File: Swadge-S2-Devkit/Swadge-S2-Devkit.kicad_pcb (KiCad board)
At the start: 2 copper layers, 134 x 100 mm, 103 parts, among them J1 CurrentMonitor, J10 LCD18, J11 LCD28, J2 DEBUG_BANK_C, J3 DEBUG_BANK_B, J4 DEBUG_BANK_A, J5 MICSEL, J6 TRYMIC, J7 LEDK_J, J8 IM0, M1 Motor_DC, P1 USB_C_Plug_USB2.0, Q1 Q_N_FET, Q2 AP2003_PN_FET, Q3 AP2003_PN_FET, Q4 AP2003_PN_FET, SW1 4-1437565-2, SW13 touch-ring-6, SW14 SW_SPDT, SW2 4-1437565-2, SW3 4-1437565-2, SW4 4-1437565-2, SW5 4-1437565-2, SW6 4-1437565-2, SW7 4-1437565-2, SW8 4-1437565-2, SW9 4-1437565-2, U1 ESP32-S2-SOLO, U10 GENERIC_LDO_GOI, U11 LCD_240x240_1.3_12, U12 LCD_135x240_1.14_13, U15 LCD_240x240_1.54_12, U2 BUS_PCIexpress, U3 MT3410, U4 GS321-TR, U5 QMA7981, U6 INGHAi_GSPK2308P-8R0.5W, U7 TFT-1.14, U8 TFT_DISPLAY, U9 GENERIC_LDO_1.8

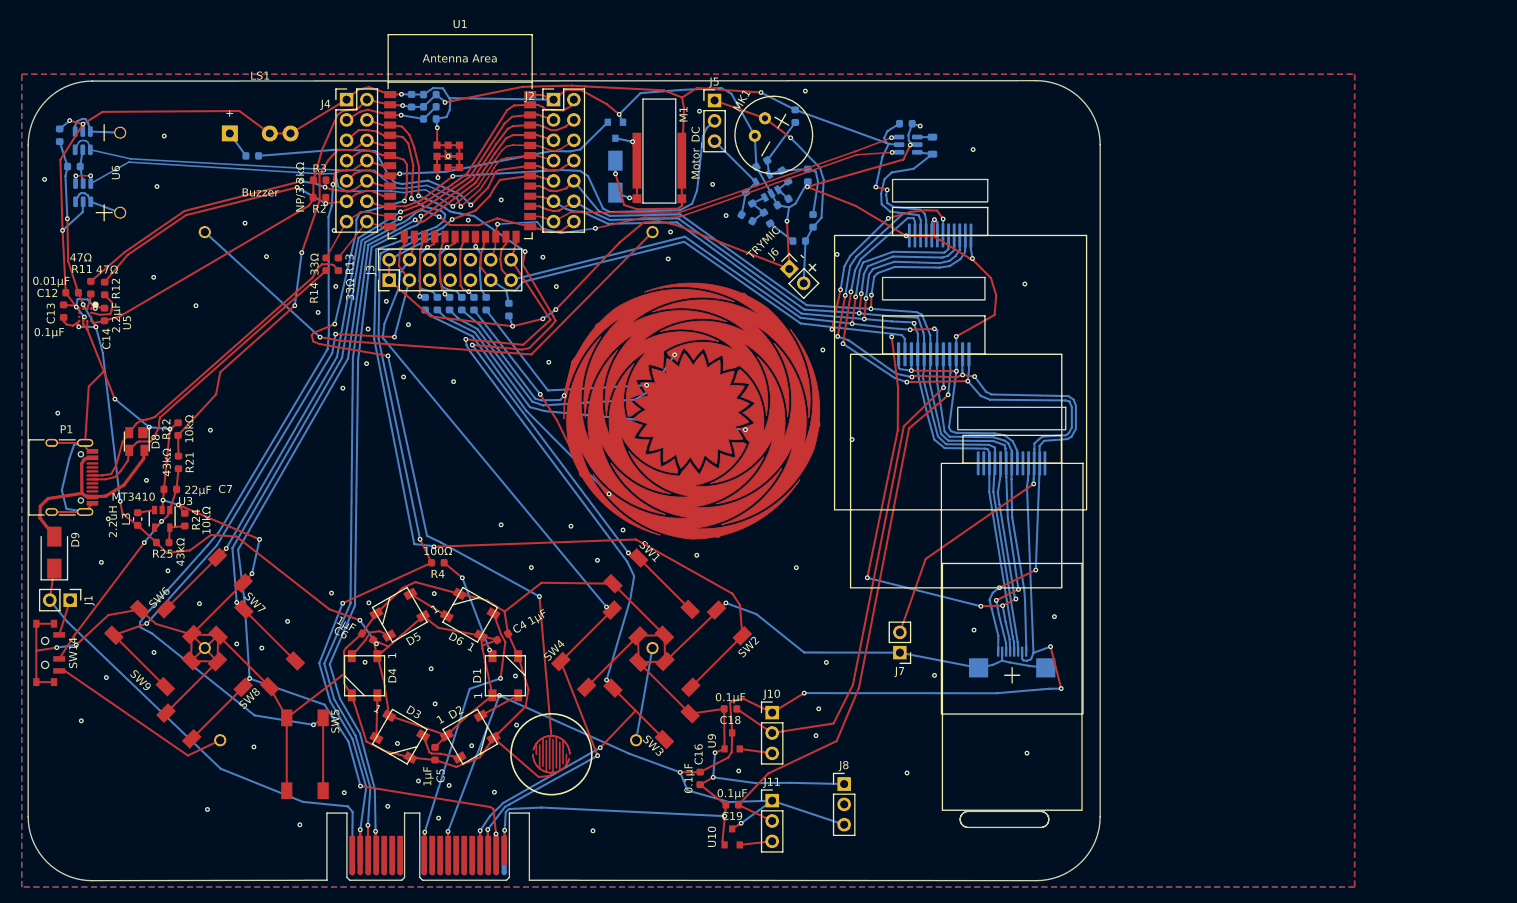
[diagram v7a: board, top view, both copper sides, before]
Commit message: Removed unused parts of schematic. Replaced out of stock parts. Rerouted batteries, LDOs
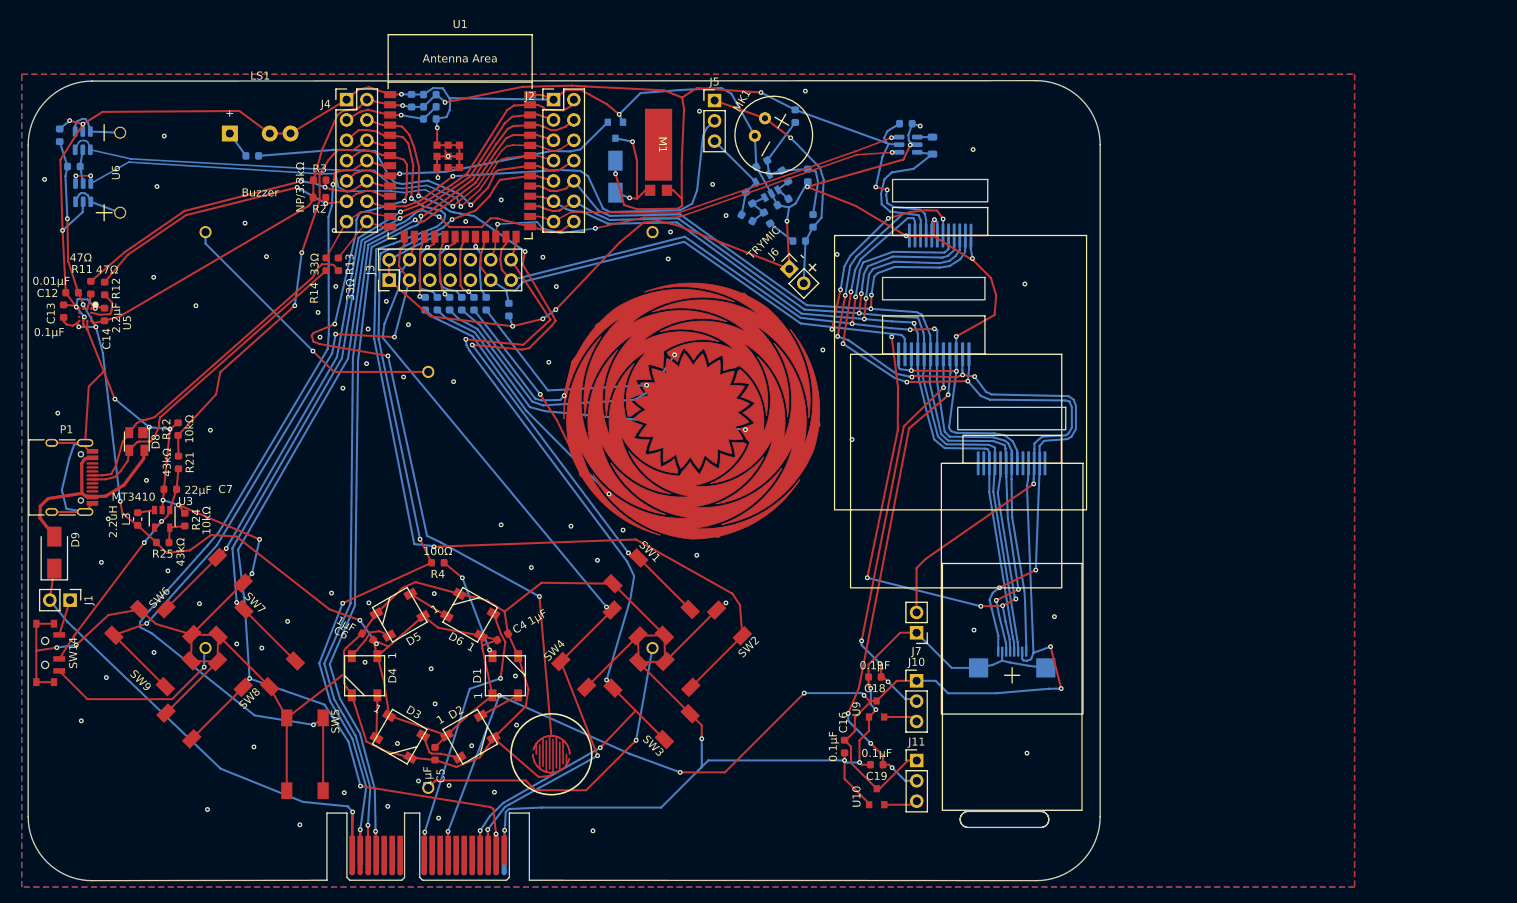
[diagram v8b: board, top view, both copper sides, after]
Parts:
- removed J8: IM0, Swadge_Parts:PinHeader_1x03_P2.54mm_Vertical
- M1: value Motor_DC -> VZ43FC1B5640007L; footprint Swadge_Parts:Z30C1B839982L -> Swadge_Parts:VZ43FC1B5640007L
- U10: value GENERIC_LDO_GOI -> GENERIC_LDO_2.8
- moved BT1 55.9 mm to (180.4, 96.5), turned to -90 degrees
- moved BT3 46.7 mm to (124.5, 96.5), turned to -90 degrees
- moved BT2 33.0 mm to (152.5, 114.0), turned to 90 degrees
- moved C19 18.8 mm to (208.5, 137.1)
- moved U10 18.8 mm to (208.5, 141.1)
- moved J11 18.8 mm to (213.5, 136.6)
- moved C18 18.5 mm to (208.2, 126.1)
- moved C16 18.5 mm to (204.4, 134.8)
- moved U9 18.5 mm to (208.4, 130.1)
- moved J10 18.5 mm to (213.4, 126.6)
- moved J7 3.24 mm to (213.4, 120.6)
- moved M1 1.50 mm to (181.2, 59.6)
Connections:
- J4 pad 6: SPARE1 -> VMON
- M1 pad 1: +3V3 -> GND
- M1 pad 2: Net-(D7-Pad2) -> +3V3
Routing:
- net BATTMID: track 67.5 -> 41.2 mm
- net BATTMID2: track 11.7 -> 35.9 mm, vias 0 -> 1
- net GND: track 814.8 -> 795.9 mm, vias 120 -> 116
- net LCD18: track 62.6 -> 49.6 mm, vias 1 -> 4
- net LCD28: track 71.3 -> 61.3 mm, vias 1 -> 4
- net +3V3: track 482.9 -> 475.4 mm
- net +5V: track 57.0 -> 62.3 mm, vias 0 -> 1
- net TFT_LEDK: track 95.6 -> 93.1 mm
- net Net-(D7-Pad2): track 12.2 -> 14.3 mm
- net BATTPLUS: track 23.8 -> 23.7 mm, vias 0 -> 1
